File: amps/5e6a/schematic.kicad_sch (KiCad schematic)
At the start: 62 parts, among them T3 part not legible

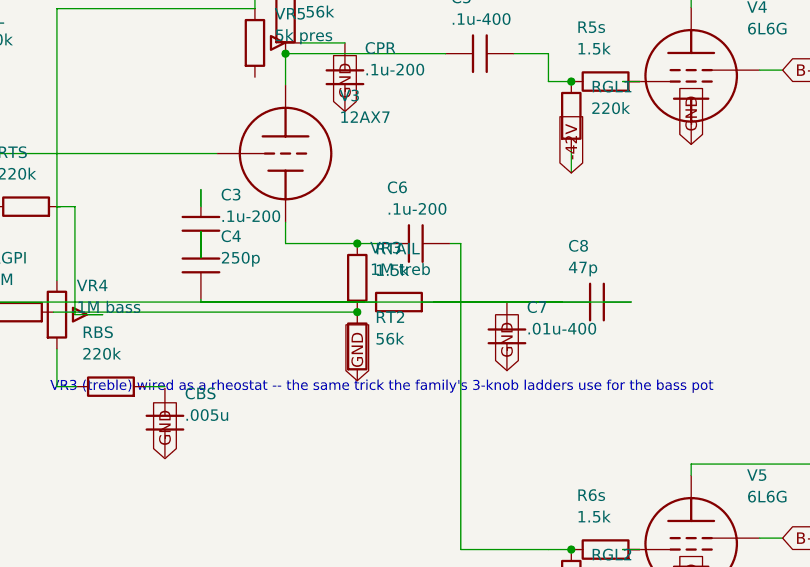
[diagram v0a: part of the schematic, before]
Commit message: Fix: eleven per-amp claims that had drifted from the circuits they describe
Prose that contradicted the corpus it sits in:

* The 5F4 called its ancestor "the 5E-series Super not yet published in this
  archive" while its own meta.yaml derives it from 5E4-A and that circuit has a
  page; the 5F1 said its lineage edge "lands when amps/5e1 exists" while the
  sidebar already links the 5E1. Both now name the documented ancestor. The
  whole corpus was swept for the pattern: 5F2-A's 5F2, 5E5-A's 5E5, 5D3's 5C3,
  5F2-A's and 5F10's earlier revisions and DR103's Sound City are all still
  genuinely absent, so those stay.
* The 5E6-A said its front end gates "within the usual tolerance (worst node
  29.8%)" against a +/-20% convention — a sentence that contradicts itself and
  understates the miss besides. It now states the four nodes that miss, the
  numbers they miss by, and the one dropper-current fault behind all four,
  which is what its own meta.yaml already said. Same defect class as the 5E4-A
  fix in 4c65fa8.
* The 5E5-A's parts list opened "No schematic.kicad_sch is authored in this
  delivery" — one has been authored. Deleted.
* Repo paths were rendering on public pages: four SOURCES entries (5F1, 5E3,
  5F2-A, 5F6, 5F6-A) named amps/<id>/layout.svg, and the 5E5-A, 5E6-A and 5F10
  pages cited voltages.yaml, netlist.cir, verify_amps.py and CONTRIBUTING.md in
  running prose. All reworded as visitor documentation. The 5F10's layout also
  described its own schematic page as "reproduced", which is the one word this
  project must never use about a factory drawing.

Circuit elements that existed only as a caption:

* The 5F6-A's headline change from the 5F6 is the presence control, and it was
  a line of schematic text. It is drawn now — 27k feedback resistor, 5k pot and
  its 0.1 uF wiper cap, at the phase-inverter tail — with designators, parts-list
  rows and chassis-edge placement on both board styles.
* The 5F4's 56k feedback and 5k presence were the same, an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
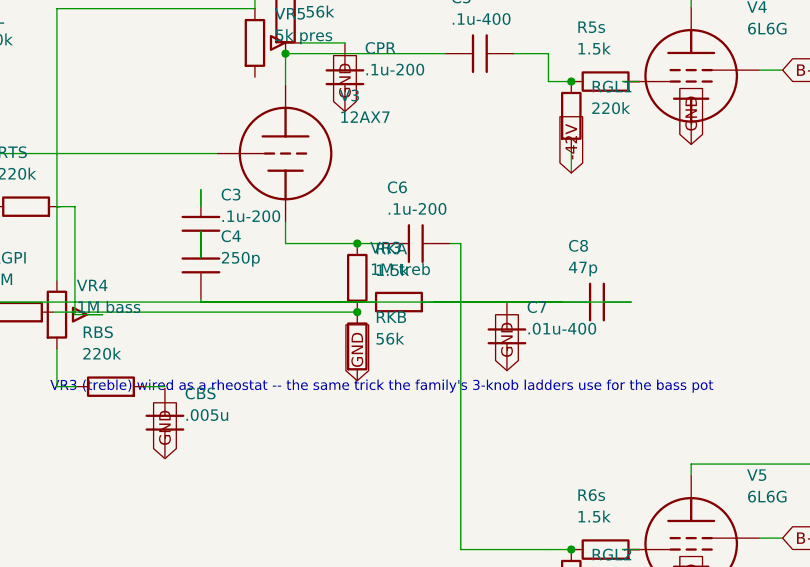
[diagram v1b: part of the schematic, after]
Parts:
- removed RT2: 56k, symbol cx:R
- removed RTAIL: 1.5k, symbol cx:R
- added RKA: 1.5k, symbol cx:R
- added RKB: 56k, symbol cx:R
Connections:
- net GND: now also RKB.2
- net at C6.1, V3.3 (K): now also RKA.1
- net at RGPI.2: now also RKA.2, RKB.1
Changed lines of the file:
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@@
   (symbol (lib_id "cx:R") (at 192.12 105.81 0) (unit 1)
     (in_bom yes) (on_board yes)
-    (property "Reference" "RTAIL" (at 194.12 102.61 0) (effects (font (size 1.27 1.27)) (justify left)))
+    (property "Reference" "RKA" (at 194.12 102.61 0) (effects (font (size 1.27 1.27)) (justify left)))
     (property "Value" "1.5k" (at 194.12 105.01 0) (effects (font (size 1.27 1.27)) (justify left))))
   (junction (at 192.12 109.62) (diameter 0) (color 0 0 0 0))
   (symbol (lib_id "cx:R") (at 192.12 113.43 0) (unit 1)
     (in_bom yes) (on_board yes)
-    (property "Reference" "RT2" (at 194.12 110.23 0) (effects (font (size 1.27 1.27)) (justify left)))
+    (property "Reference" "RKB" (at 194.12 110.23 0) (effects (font (size 1.27 1.27)) (justify left)))
     (property "Value" "56k" (at 194.12 112.63 0) (effects (font (size 1.27 1.27)) (justify left))))
   (global_label "GND" (shape input) (at 192.12 117.24 270)

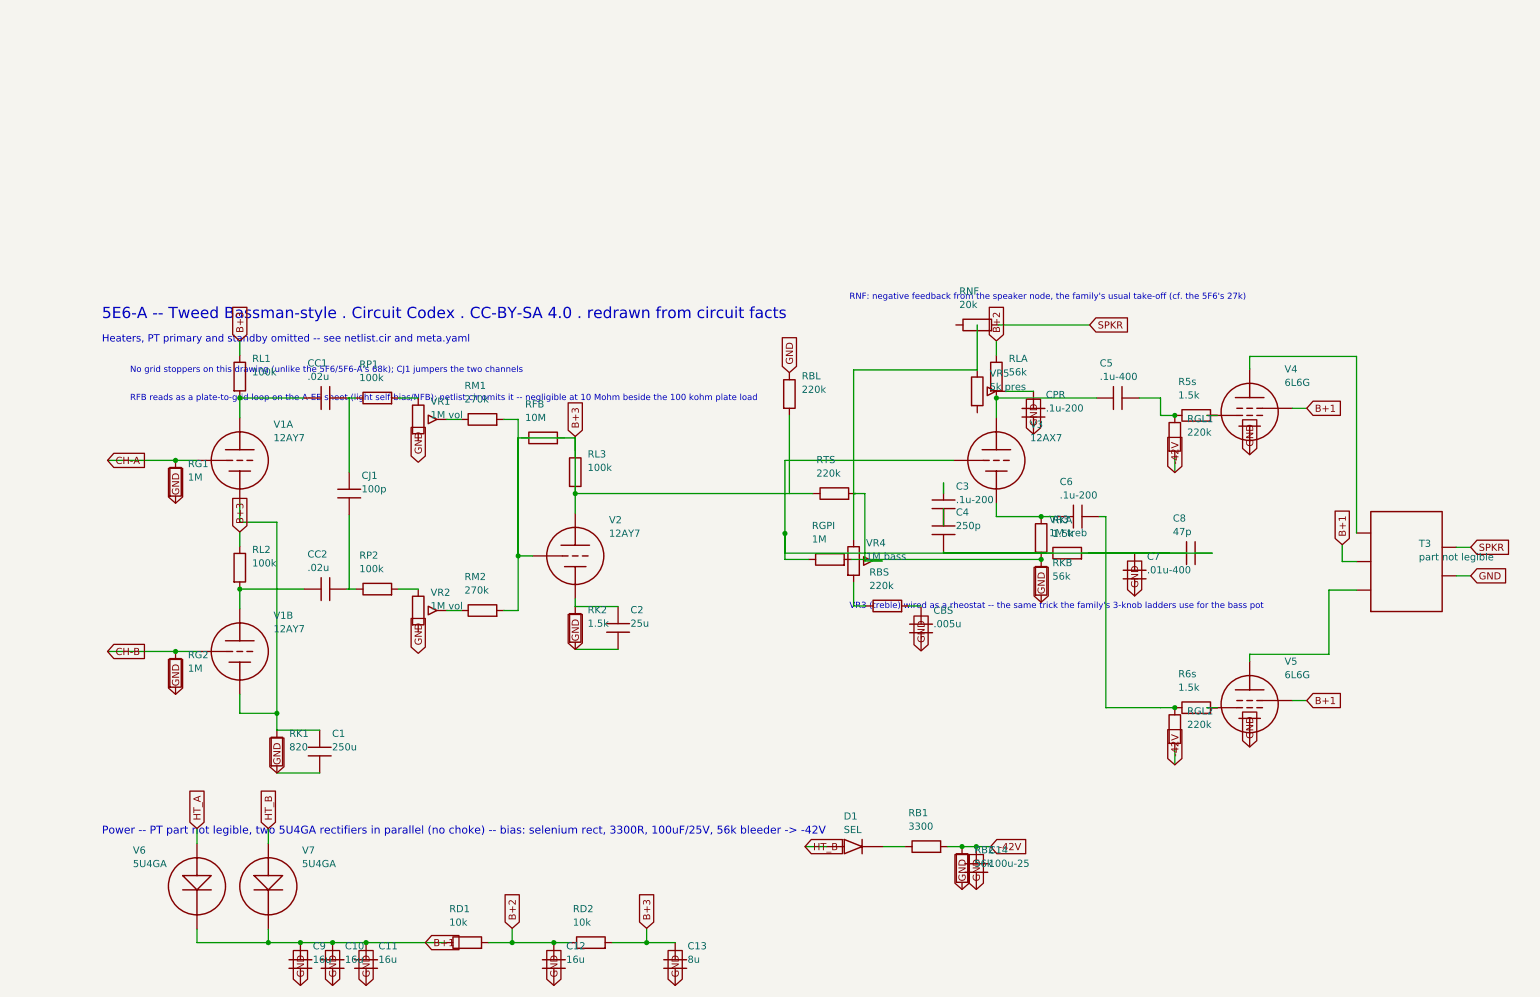
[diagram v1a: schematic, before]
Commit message: Update: regenerate every drawing the four merged units changed
The four parallel units all rewrote generators, so their committed artifacts
were each generated against only their own third of the merged pipeline. Every
schematic, both layout styles, the social cards and the manifest are rebuilt
here from the merged sources, so what ships is what the merged generators draw.

One integration fault the rebuild exposed, invisible to any single unit:

- 5E5-A: the note explaining that the Presence wiper and the 100k feedback
  resistor land on V3A's GRID (not its cathode, as on the 5F4) was added as a
  hand-placed `s.text()` at a coordinate chosen before the sheet gained a
  reserved notes band. Merged, it printed through the -32V bias label. Moved to
  `note()`, which wraps prose into that band — the exact failure mode the band
  was built to end.

Three conflicts resolved against docs/lettering-conventions.md rather than by
picking a side, since two units had corrected the same lines for different
reasons:

- 5E5-A tone/feedback caps take the corrected designators (C7, C8, C9, RNF —
  `C_tr1`/`C_NFB` were generator identifiers that had leaked onto a published
  board) with the house-derived lettering (`.01u 400V`, `500p`, `.1u 200V`).
  Dropping the working voltage or writing `.0005u` would have lost a rating the
  source prints and re-broken the pF/µF decade rule.
- 5D3 C6 and 6G6-B's three cathode resistors take the SI-prefix form the
  convention binds (`.005u`, `2.7k`, `1.5k`), keeping the ground-flag direction
  fix and the removal of the second `gnd()` that shorted each cathode it biased.
- 5F6-A's bias supply keeps both 8 µF cans drawn — the second was previously a
  parenthetical claiming one of two was shown — at the coordinates that clear
  the title-block strip.

All gates green, including check_value_consistency at zero disagreements.

🤖 Generated with [Claude Code](https://claude.com/claude-code)

Co-Authored-By: Claude Fable 5 <noreply@anthropic.com>
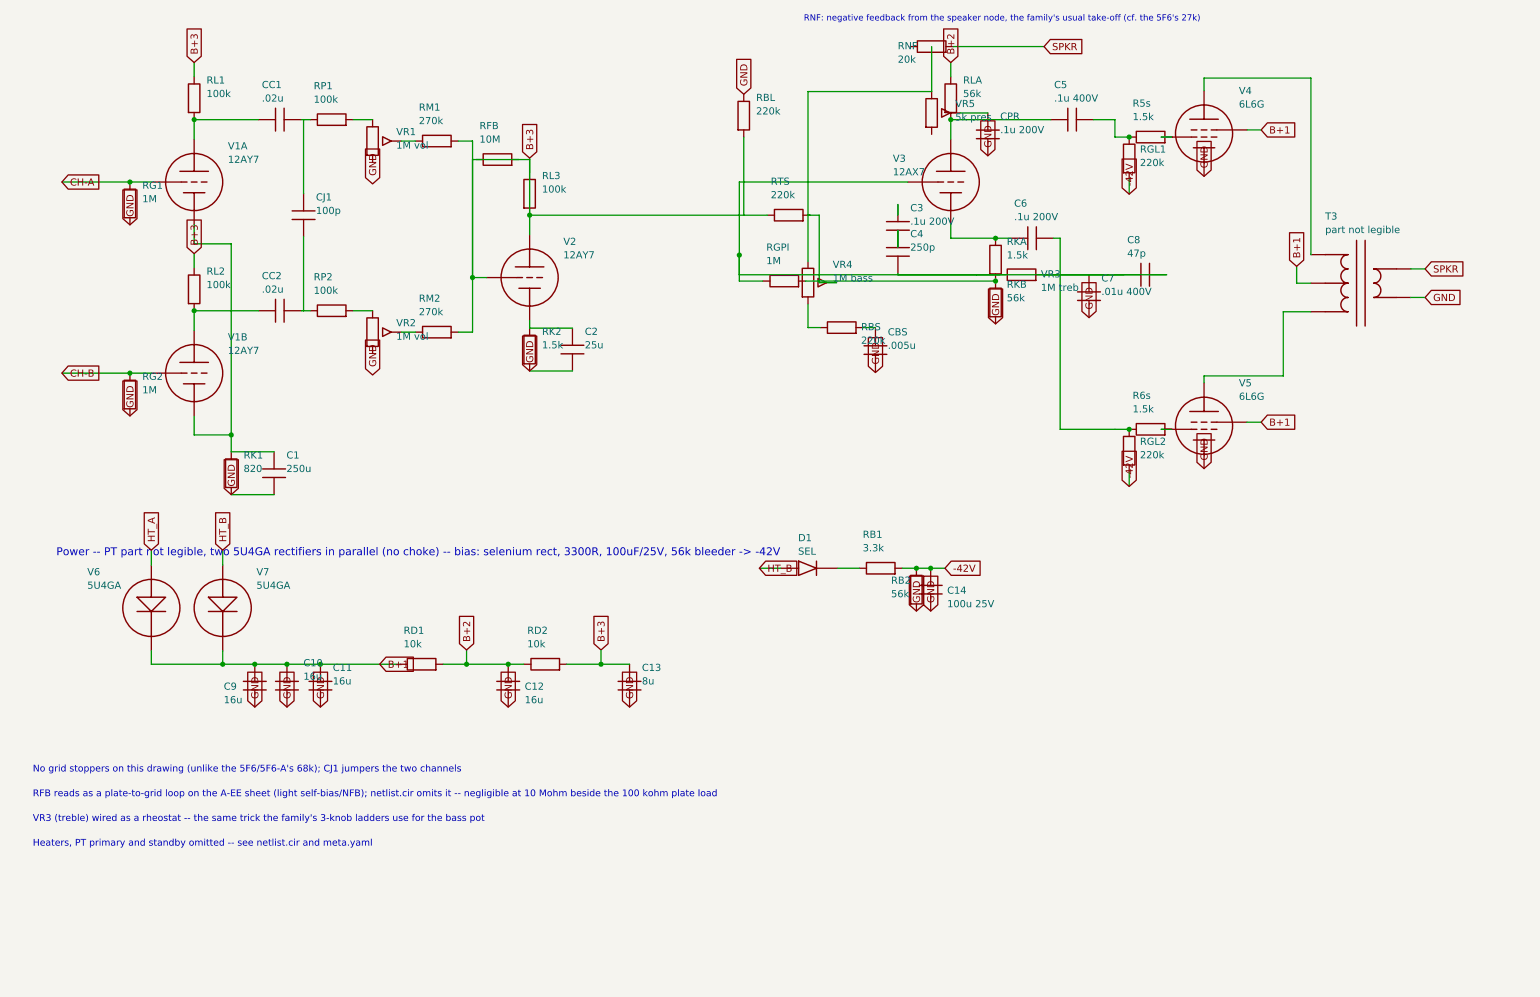
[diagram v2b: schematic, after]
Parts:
- C14: value 100u-25 -> 100u 25V
- C3, C6, CPR: value .1u-200 -> .1u 200V
- C5: value .1u-400 -> .1u 400V
- C7: value .01u-400 -> .01u 400V
- RB1: value 3300 -> 3.3k
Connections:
- net B+3: no longer V2.2 (G)
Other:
- note removed: "5E6-A -- Tweed Bassman-style . Circuit Codex . CC-BY-SA 4.0 . redrawn from circuit facts"
- company: (none) -> Circuit Codex
- title: (none) -> 5E6-A — Tweed Bassman-style

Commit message: Fix: rotated global labels lettered their net names outside the flag
Every global label this pipeline emitted carried (justify left) regardless of
rotation. KiCanvas — like KiCad — draws label text horizontally at 0/180 and
vertically at 90/270 and reads WHICH SIDE of the anchor it letters on from the
justification, so at 180 and 270 the name printed outside an empty flag
outline, struck through by the very wire it names: 219 labels at 180 deg
(including the input-jack flags at top-left of nearly every sheet, the first
glyphs a visitor reads) and 792 GND/rail flags at 270 whose names squeezed at
the flag mouth instead of lettering down the body. The library already
compensated rotation for property text (`pa`); this mirrors that logic for
global labels: justify right at 180/270, left at 0/90.

check_schematics gains the geometry clause whose absence let all 1011
instances through a "no lettering through circuitry" pass: it modelled the
flag box but never the label TEXT, so a name rendered on the wrong side was
invisible to it. The gate now proves justification compensates rotation on
every global label.

Two more things this exposed, fixed in the same engine pass:

- Placement now measures with the renderer's own Newstroke advance table
  (extracted from the vendored kicanvas.js) instead of a flat 0.68-em prose
  average that under-read part lettering by a quarter — the mechanism behind
  every "metered clean, printed through its neighbour" incident. The GATE
  deliberately keeps the coarse ruler: re-ruling it with renderer truth was
  tried and red-flagged 28 of 34 sheets over abutments three visual passes
  had already judged sub-visual (the two-rulers note in schematic_lib.py).
- place_captions' escape ladder runs further, because a banner caption
  measured truly is half again wider than the old estimate believed.

All 34 schematics regenerated; full gate suite green.

🤖 Generated with [Claude Code](https://claude.com/claude-code)

Co-Authored-By: Claude Fable 5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
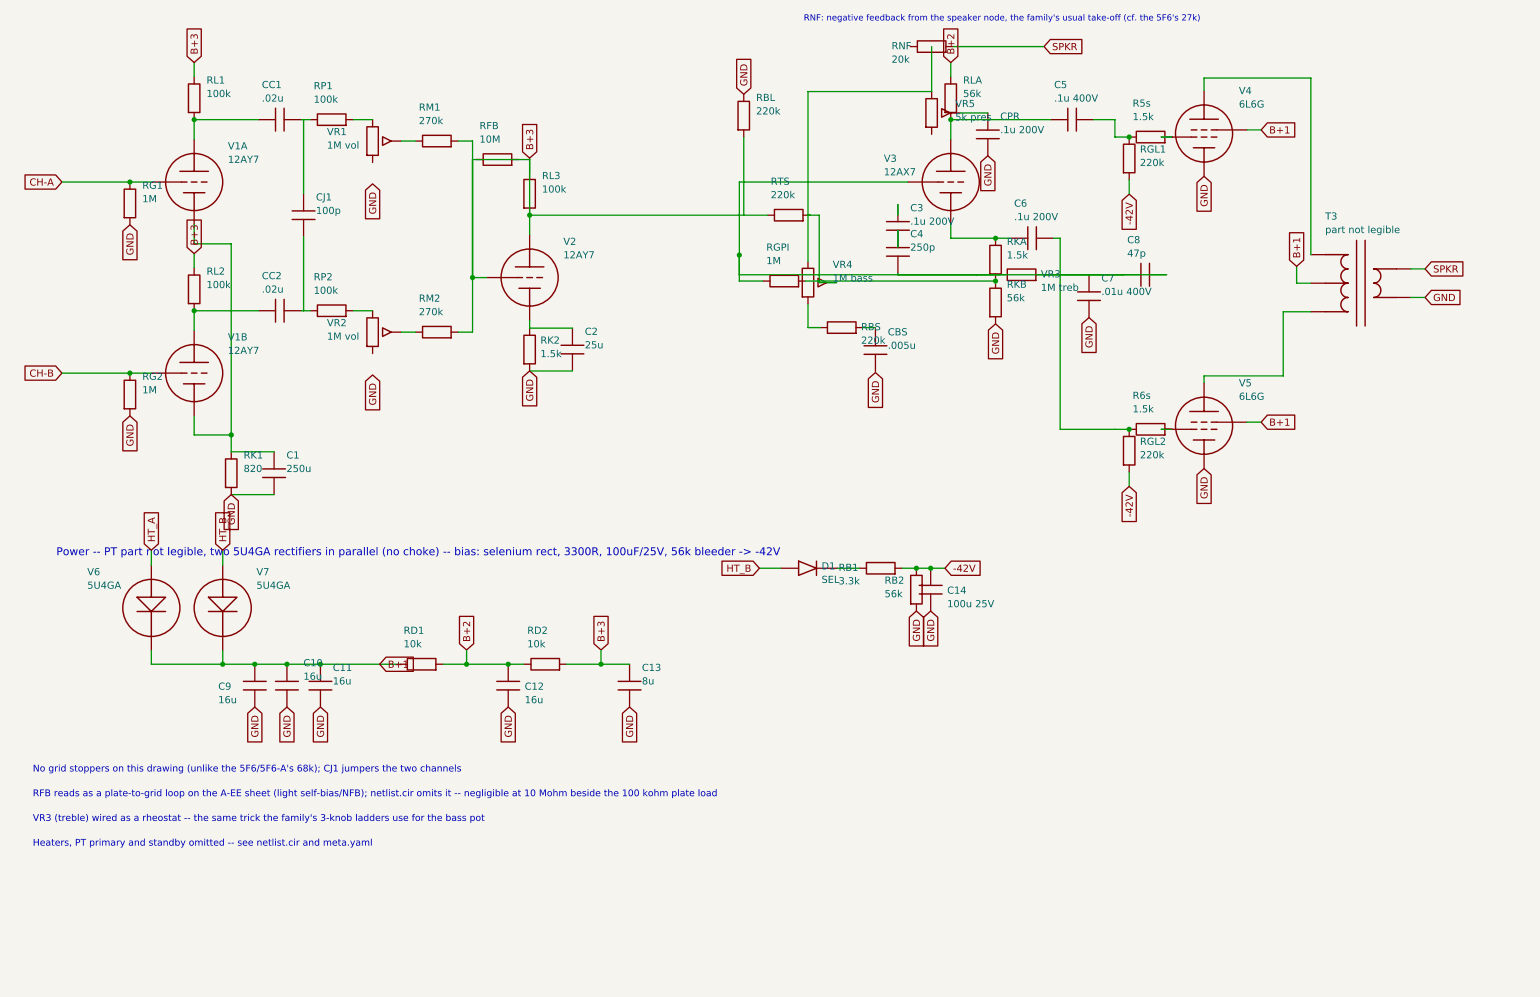
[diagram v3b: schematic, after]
